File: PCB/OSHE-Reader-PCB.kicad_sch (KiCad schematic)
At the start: 11 parts

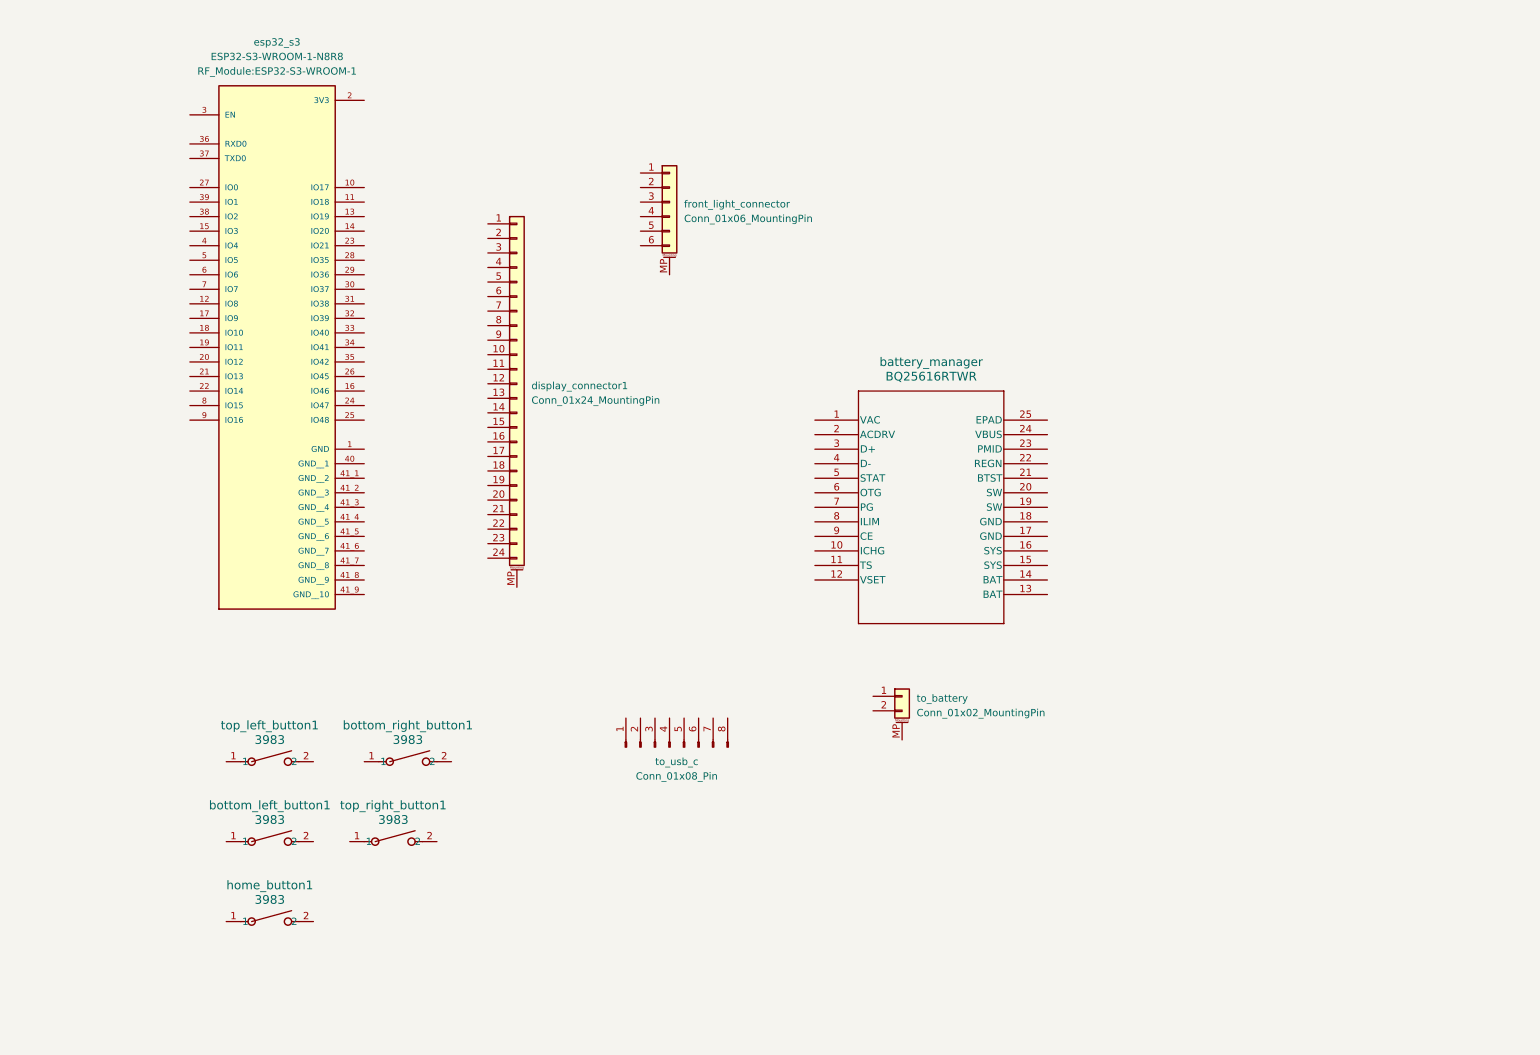
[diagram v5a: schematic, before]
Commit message: Labeled connectors
- display connector mostly done
- labeled pins of most external connectors
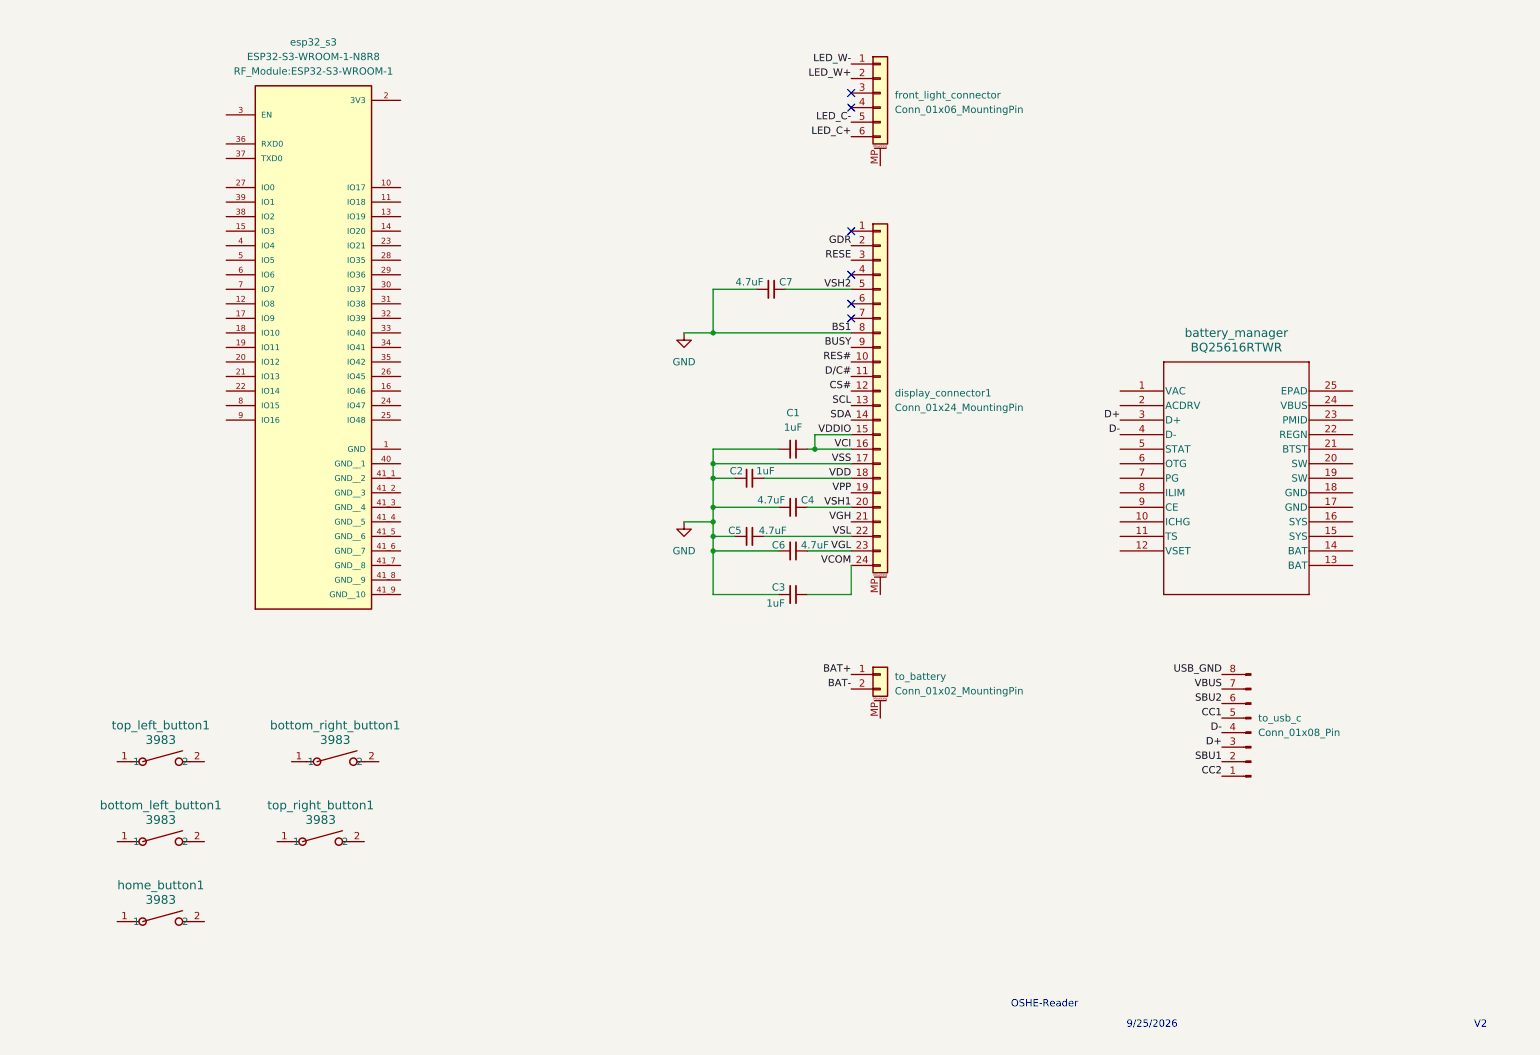
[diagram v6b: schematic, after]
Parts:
- added C1, C2, C3: 1uF, Capacitor_SMD:C_1206_3216Metric_Pad1.33x1.80mm_HandSolder, symbol Device:C_Small
- added C4, C5, C6, C7: 4.7uF, Capacitor_SMD:C_1206_3216Metric_Pad1.33x1.80mm_HandSolder, symbol Device:C_Small
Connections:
- net RES#: now reaches display_connector1.10 (Pin_10)
- net D/C#: now reaches display_connector1.11 (Pin_11)
- net CS#: now reaches display_connector1.12 (Pin_12)
- net SCL: now reaches display_connector1.13 (Pin_13)
- net SDA: now reaches display_connector1.14 (Pin_14)
- net VCI: now reaches display_connector1.15 (Pin_15)
- net VCI: now also display_connector1.16 (Pin_16), C1.2
- net GND: now reaches display_connector1.17 (Pin_17)
- net GND: now also display_connector1.8 (Pin_8), C1.1, C2.2, C3.1, C4.1, C5.1, C6.1, C7.1
- net VDD: now reaches display_connector1.18 (Pin_18)
- net VDD: now also C2.1
- net VPP: now reaches display_connector1.19 (Pin_19)
- net GDR: now reaches display_connector1.2 (Pin_2)
- net VSH1: now reaches display_connector1.20 (Pin_20)
- net VSH1: now also C4.2
- net VGH: now reaches display_connector1.21 (Pin_21)
- net VSL: now reaches display_connector1.22 (Pin_22)
- net VSL: now also C5.2
- net VGL: now reaches display_connector1.23 (Pin_23)
- net VGL: now also C6.2
- net VCOM: now reaches display_connector1.24 (Pin_24)
- net VCOM: now also C3.2
- net RESE: now reaches display_connector1.3 (Pin_3)
- net VSH2: now reaches display_connector1.5 (Pin_5)
- net VSH2: now also C7.2
- net BUSY: now reaches display_connector1.9 (Pin_9)
- net BAT+: now reaches to_battery.1 (Pin_1)
- net BAT-: now reaches to_battery.2 (Pin_2)
- net LED_W-: now reaches front_light_connector.1 (Pin_1)
- net LED_W+: now reaches front_light_connector.2 (Pin_2)
- net LED_C-: now reaches front_light_connector.5 (Pin_5)
- net LED_C+: now reaches front_light_connector.6 (Pin_6)
- net D+: now reaches battery_manager.3 (D+)
- net D+: now also to_usb_c.3 (Pin_3)
- net D-: now reaches battery_manager.4 (D-)
- net D-: now also to_usb_c.4 (Pin_4)
- net CC2: now reaches to_usb_c.1 (Pin_1)
- net SBU1: now reaches to_usb_c.2 (Pin_2)
- net CC1: now reaches to_usb_c.5 (Pin_5)
- net SBU2: now reaches to_usb_c.6 (Pin_6)
- net VBUS: now reaches to_usb_c.7 (Pin_7)
- net USB_GND: now reaches to_usb_c.8 (Pin_8)
- no-connect marks 0 -> 6
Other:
- note added: "9/25/2026"
- note added: "OSHE-Reader"
- note added: "V2"
- moved on the sheet: battery_manager, bottom_left_button1, bottom_right_button1, display_connector1, esp32_s3, front_light_connector, home_button1, to_battery, to_usb_c, top_left_button1, top_right_button1

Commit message: Working on schematic
The display schematic should be done now
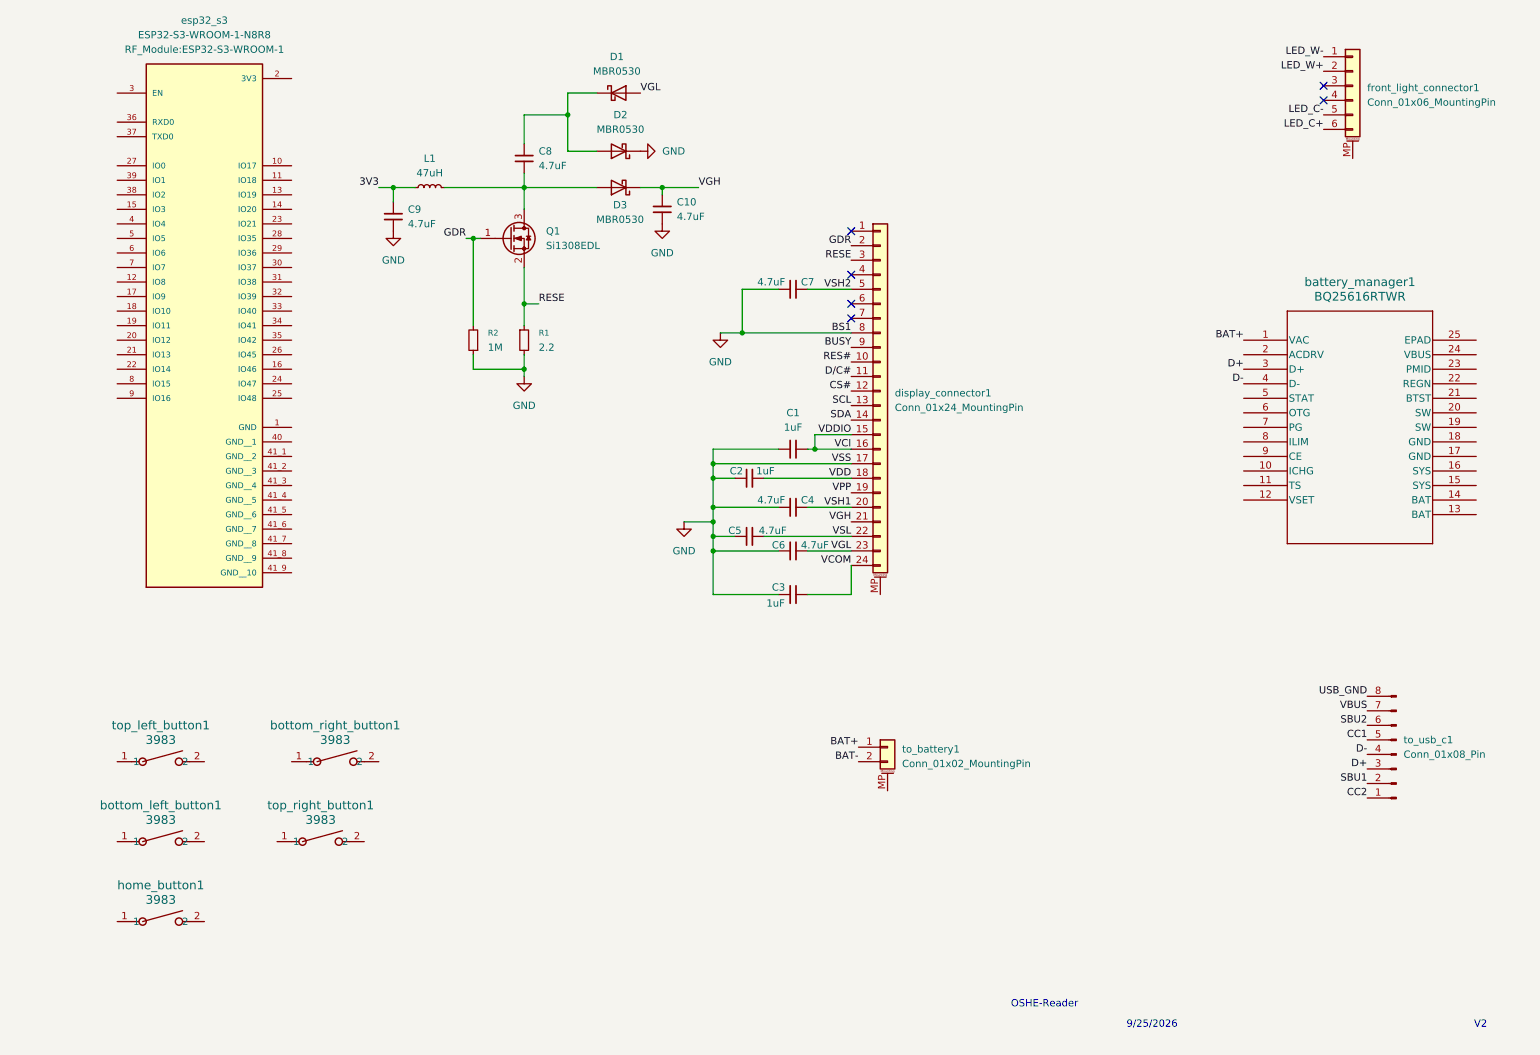
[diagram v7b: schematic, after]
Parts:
- added C10, C8, C9: 4.7uF, Package_TO_SOT_SMD:SOT-23-6, symbol Device:C_Small
- added D1, D2, D3: MBR0530, Diode_SMD:D_SOD-123, symbol Diode:MBR0530
- added L1: 47uH, Package_SO:SOIC-20W_7.5x12.8mm_P1.27mm, symbol Device:L_Small
- added Q1: Si1308EDL, Package_TO_SOT_SMD:SOT-323_SC-70, symbol Transistor_FET:Si1308EDL
- added R1: 2.2, Package_TO_SOT_SMD:SOT-323_SC-70, symbol Device:R_Small
- added R2: 1M, symbol Device:R_Small
- renumbered battery_manager to battery_manager1, front_light_connector to front_light_connector1, to_battery to to_battery1, to_usb_c to to_usb_c1
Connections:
- net BAT+: now also battery_manager1.1 (VAC)
- net GDR: now also Q1.1 (G), R2.2
- net GND: now also C10.2, C9.2, D2.1 (K), R1.2, R2.1
- net RESE: now also Q1.2 (S), R1.1
- net VGH: now also C10.1, D3.1 (K)
- net VGL: now also D1.2 (A)
- new net: C8.1, D1.1 (K), D2.2 (A)
- new net: C8.2, D3.2 (A), L1.2, Q1.3 (D)
- new net 3V3: C9.1, L1.1
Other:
- moved on the sheet: C7, battery_manager1, esp32_s3, front_light_connector1, to_battery1, to_usb_c1

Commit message: Buttons complete
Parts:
- added R3, R4, R5, R6, R7: 10k, Resistor_SMD:R_1206_3216Metric_Pad1.30x1.75mm_HandSolder, symbol Device:R_Small
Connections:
- net 3V3: now also esp32_s3.2 (3V3), R3.1, R4.1, R5.1, R6.1, R7.1
- net GND: now also bottom_left_button1.2, bottom_right_button1.2, esp32_s3.1 (GND), home_button1.2, top_left_button1.2, top_right_button1.2
- net HOME_button: now reaches home_button1.1
- net HOME_button: now also esp32_s3.12 (IO8), R7.2
- net BL_button: now reaches bottom_left_button1.1
- net BL_button: now also esp32_s3.6 (IO6), R6.2
- net TL_button: now reaches top_left_button1.1
- net TL_button: now also esp32_s3.7 (IO7), R5.2
- net BR_button: now reaches bottom_right_button1.1
- net BR_button: now also esp32_s3.4 (IO4), R3.2
- net TR_button: now reaches top_right_button1.1
- net TR_button: now also esp32_s3.5 (IO5), R4.2
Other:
- note added: "Buttons"
- note added: "Display + Front Light"
- moved on the sheet: C1, C10, C2, C3, C4, C5, C6, C7, C8, C9, D1, D2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
